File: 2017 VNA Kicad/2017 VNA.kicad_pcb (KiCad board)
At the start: 2 copper layers, 50 x 30 mm, 48 parts, among them P1 Output, P2 Input, U1 SI5351A, U2 NL7WB66, Y1 CX3225

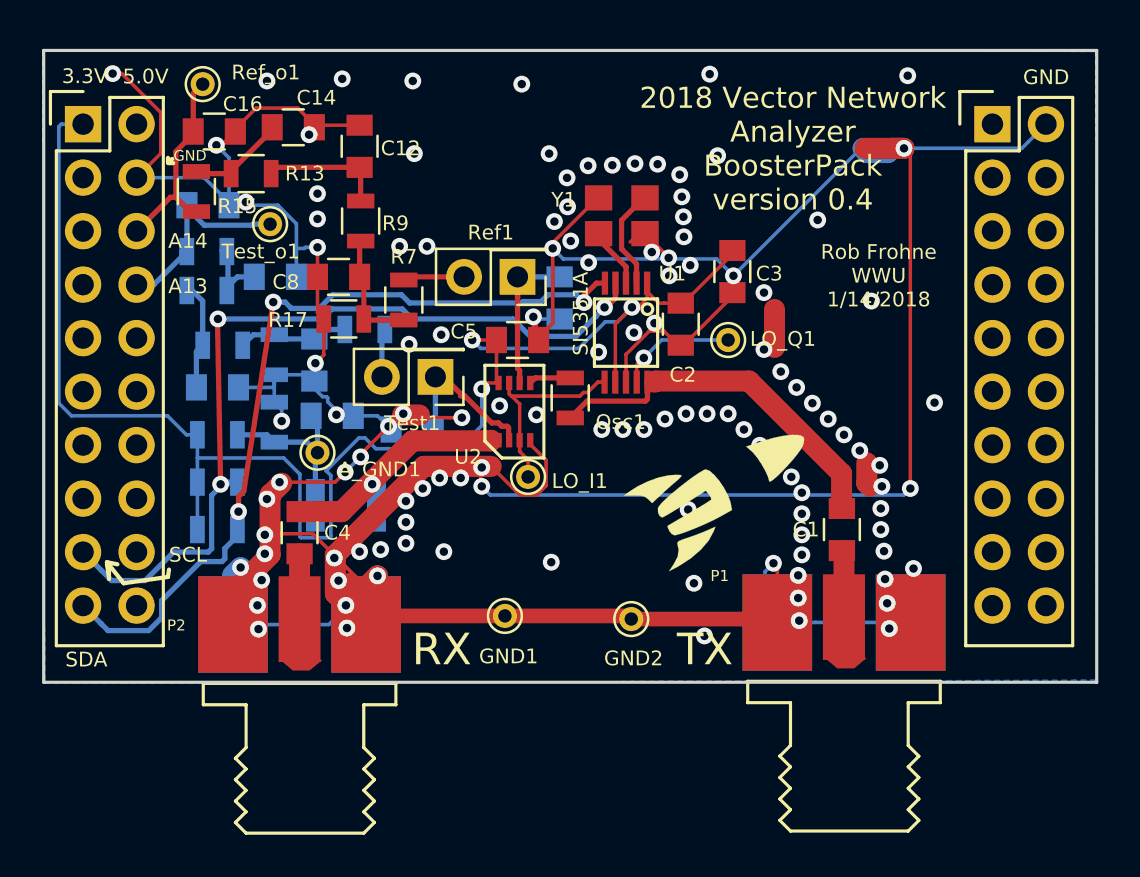
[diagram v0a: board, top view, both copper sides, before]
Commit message: Put all of the filtering components on top
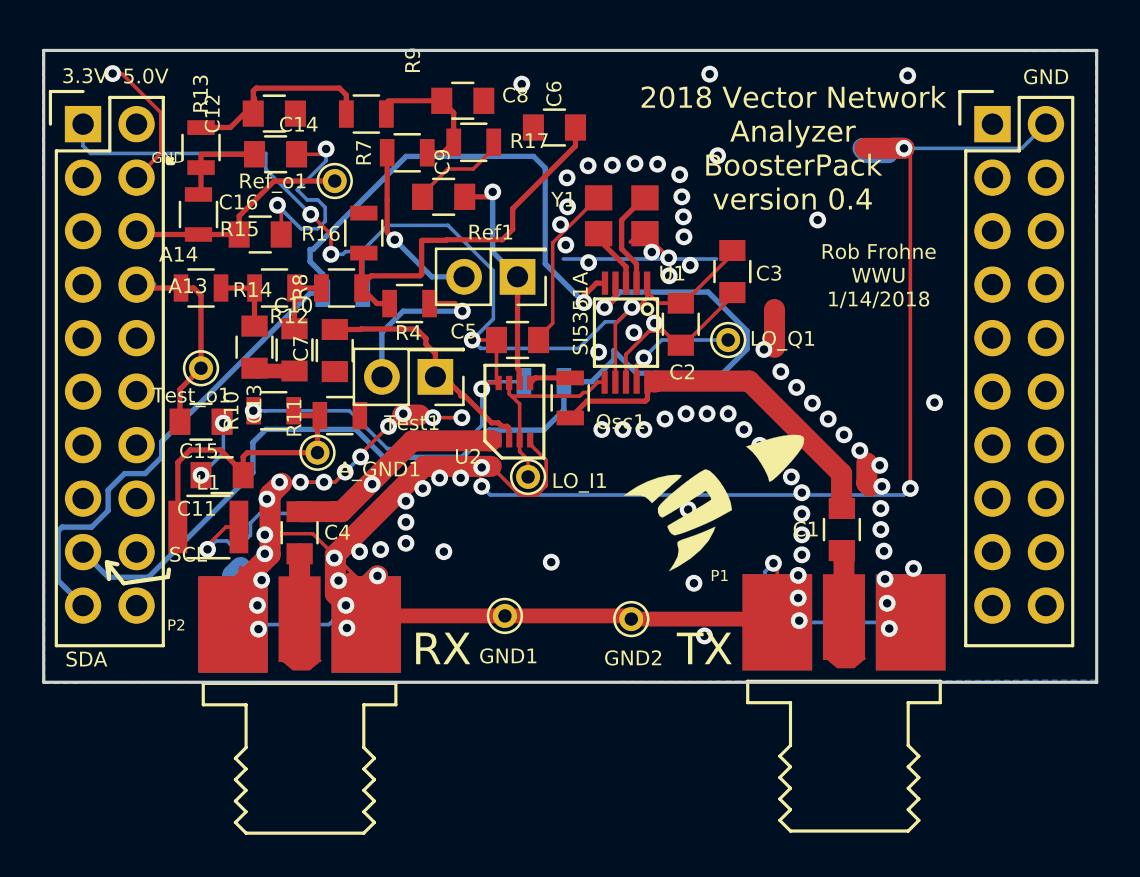
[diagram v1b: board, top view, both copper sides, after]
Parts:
- C10, C11, C13, C15, C6, C7, C9, L1, R10, R11, R12, R14, R16, R4, R8: moved to F.Cu
- moved R1 16.2 mm to (93.8, 85.7)
- moved C6 15.9 mm to (94.2, 73.7), turned to 180 degrees
- moved R2 12.7 mm to (84.2, 81.5), turned to 0 degrees
- moved R17 10.4 mm to (90.4, 74.4), turned to 0 degrees
- moved C15 10.3 mm to (77.5, 87.6)
- moved C8 10.2 mm to (89.9, 72.4), turned to 0 degrees
- moved Ref_o1 7.78 mm to (83.8, 76.2)
- moved Test_o1 7.59 mm to (77.5, 85.1)
- moved C9 7.31 mm to (89.0, 77.0), turned to 180 degrees
- moved R16 7.17 mm to (85.2, 78.7), turned to 90 degrees
- moved R7 6.99 mm to (87.3, 74.9), turned to 180 degrees
- moved L1 6.61 mm to (77.8, 92.6)
- moved R8 6.26 mm to (84.1, 81.3)
- moved C11 5.94 mm to (78.5, 90.2), turned to 180 degrees
- moved C16 5.35 mm to (80.3, 78.7)
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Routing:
- net GND: track 246.1 -> 211.0 mm, vias 122 -> 103
- net Net-(C6-Pad1): track 5.95 -> 18.8 mm
- net /Test_In: track 14.3 -> 24.8 mm, vias 1 -> 2
- net /SCL: track 41.1 -> 50.5 mm, vias 3 -> 1
- net /SDA: track 39.2 -> 46.5 mm, vias 3 -> 1
- net Net-(A_GND1-Pad1): track 8.57 -> 14.8 mm
- net Net-(R4-Pad2): track 2.31 -> 8.06 mm, vias 0 -> 1
- net Net-(R7-Pad2): track 2.92 -> 8.30 mm, vias 0 -> 1
- net Net-(C9-Pad1): track 7.33 -> 11.5 mm, vias 0 -> 1
- net Net-(C12-Pad1): track 5.94 -> 9.85 mm
- net Net-(C7-Pad1): track 7.68 -> 11.2 mm
- net +3V3: track 74.6 -> 71.7 mm, vias 3 -> 6
- net Net-(C10-Pad1): track 5.78 -> 3.22 mm
- net /A14: track 9.69 -> 11.0 mm
- net /A13: track 9.62 -> 10.8 mm

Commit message: Added Ferrit beads to input and output of ADC
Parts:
- added FB1: Ferrite_Bead, Inductors_SMD:L_0805, F.Cu at (77.6, 80.3)
- added FB2: Ferrite_Bead, Inductors_SMD:L_0805, F.Cu at (77.9, 77.5)
- C11: value 10uF -> 0pF
- C12: value 0.1uF -> 1nF
- C6: value 1uF -> 1nF
- R10: value 16k -> 330
- R11: value 10k -> 220
- R16: value 160 -> 16k
- R4: value 51 -> 5.1k
- moved R15 2.99 mm to (77.3, 74.8)
- moved R13 2.36 mm to (77.7, 72.3), turned to 0 degrees
- moved R14 1.65 mm to (77.5, 82.9)
- moved C16 0.80 mm to (80.5, 79.5)
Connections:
- R4 pad 2: Net-(R4-Pad2) -> Net-(JP_Test1-Pad2)
- R7 pad 2: Net-(R7-Pad2) -> Net-(JP_Ref1-Pad2)
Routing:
- net GND: track 211.0 -> 229.2 mm
- net /A13: track 10.8 -> 16.5 mm
- net Net-(R7-Pad2): track 8.30 -> 4.02 mm
- net /A14: track 11.0 -> 15.0 mm
- net Net-(R4-Pad2): track 8.06 -> 6.35 mm
- net Net-(C12-Pad1): track 9.85 -> 8.81 mm
- net Net-(C14-Pad1): track 4.48 -> 5.01 mm
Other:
- board text added: "Jake Neal & Andrew Glencross WWU 05/28/2018"
- board text removed: "Rob Frohne WWU 1/14/2018"

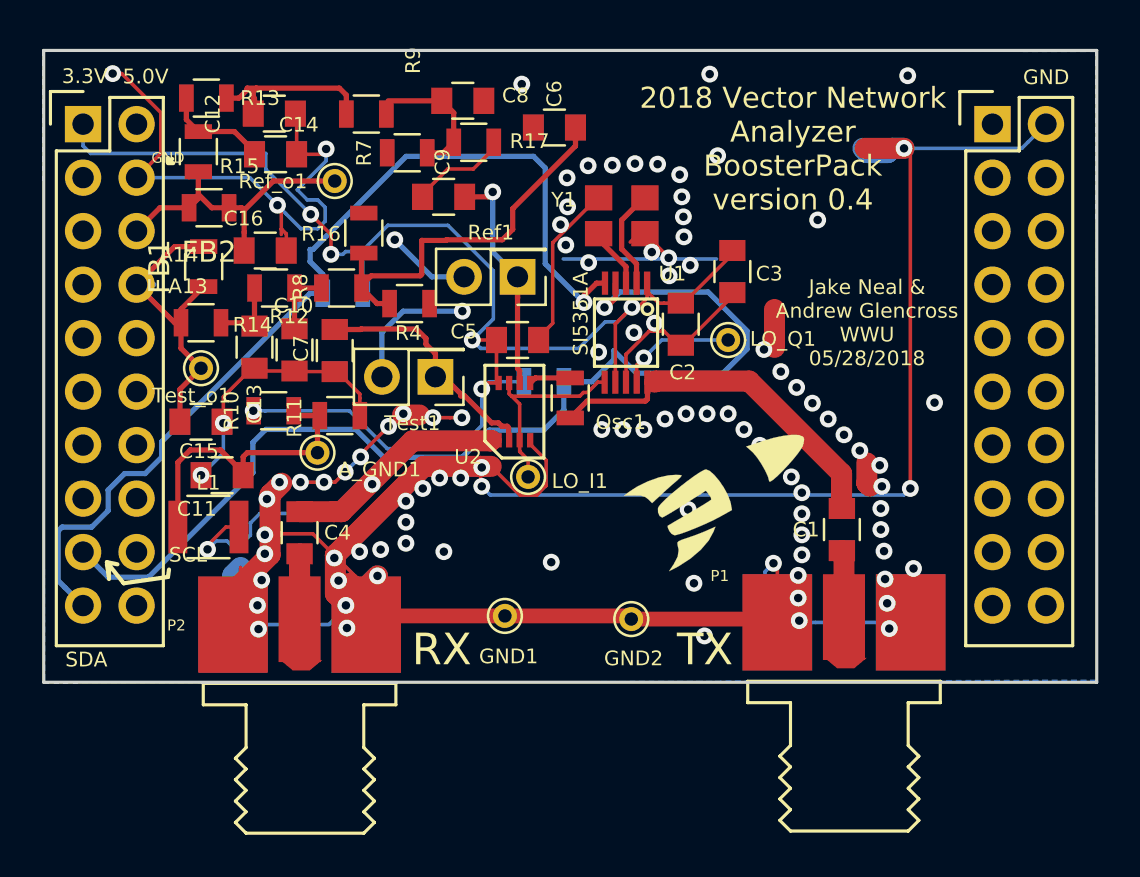
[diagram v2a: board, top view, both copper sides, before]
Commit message: Fixed version number and orientation of component labels
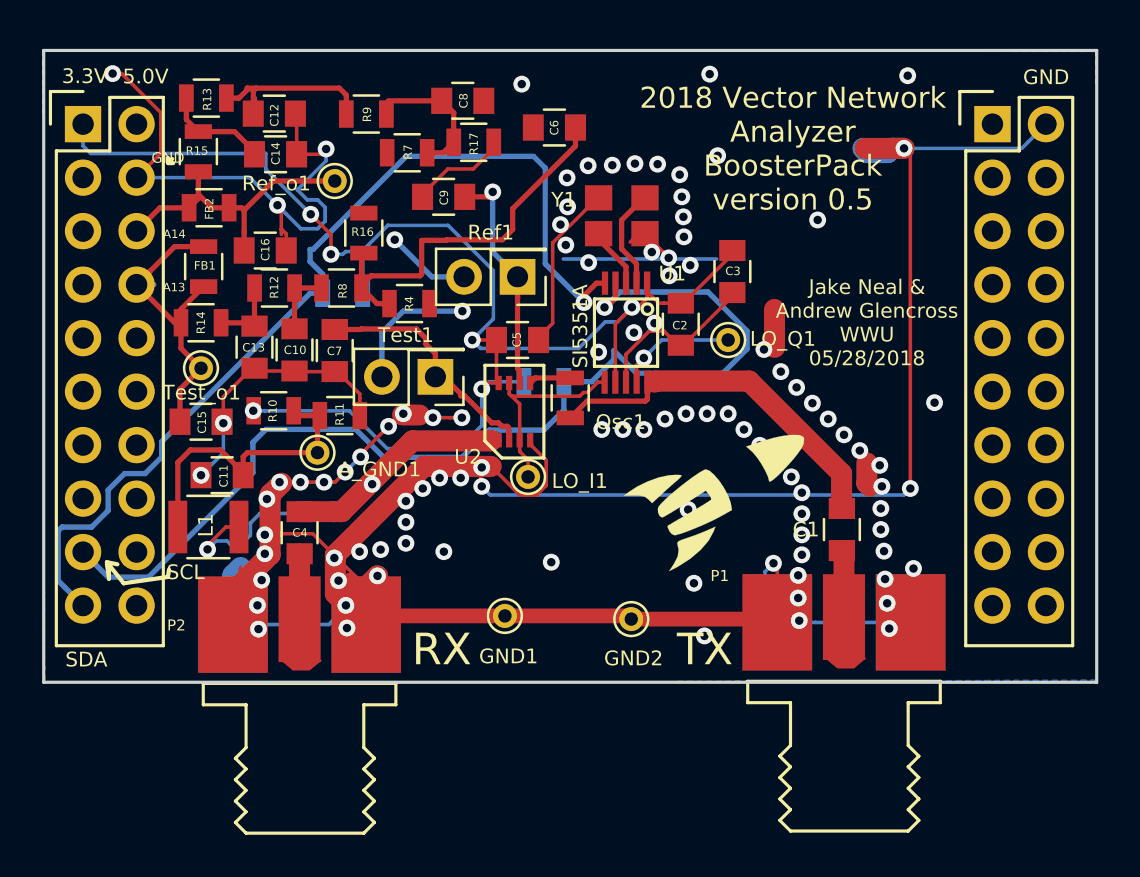
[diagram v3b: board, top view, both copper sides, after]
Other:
- board text added: "2018 Vector Network Analyzer BoosterPack version 0.5"
- board text removed: "2018 Vector Network Analyzer BoosterPack version 0.4"

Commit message: Actually changed the version number this time. Filled in ground planes and other cosmetic issues.
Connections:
- R4 pad 2: Net-(JP_Test1-Pad2) -> Net-(R4-Pad2)
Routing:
- net +3V3: track 71.7 -> 71.2 mm
- net GND: vias 103 -> 110
